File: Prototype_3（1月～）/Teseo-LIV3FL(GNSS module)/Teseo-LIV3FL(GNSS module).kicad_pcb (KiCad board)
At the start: 2 copper layers, 17 x 27.5 mm, 9 parts, among them IC1 TESEO-LIV3FL, J1 Conn_Coaxial, J2 Conn_01x05_Pin

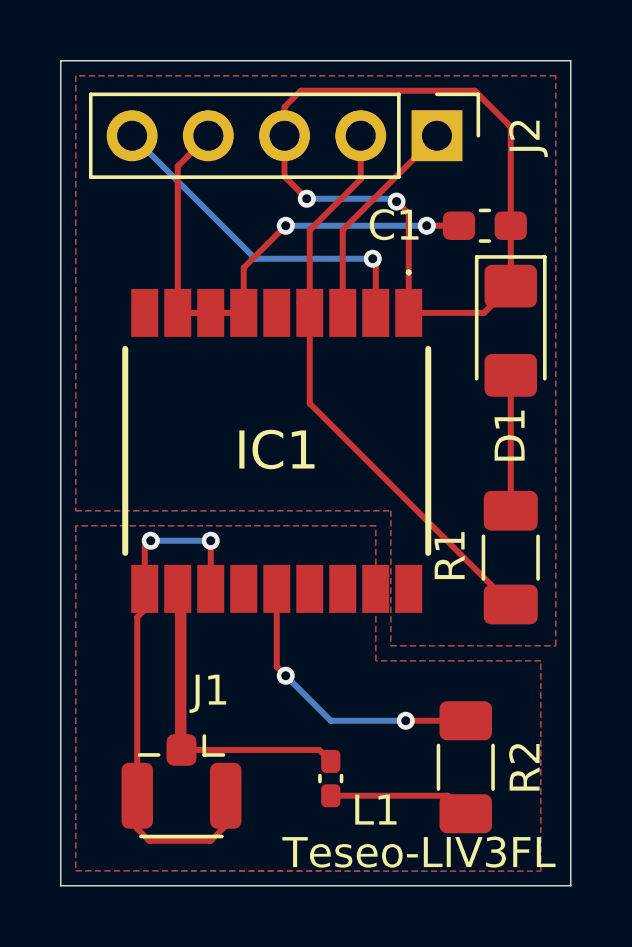
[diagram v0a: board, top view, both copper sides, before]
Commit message: Teseo
シルク印刷修正
- ピン名
シルク印刷追加
- LED Anode端子
- IC1 pin1丸印
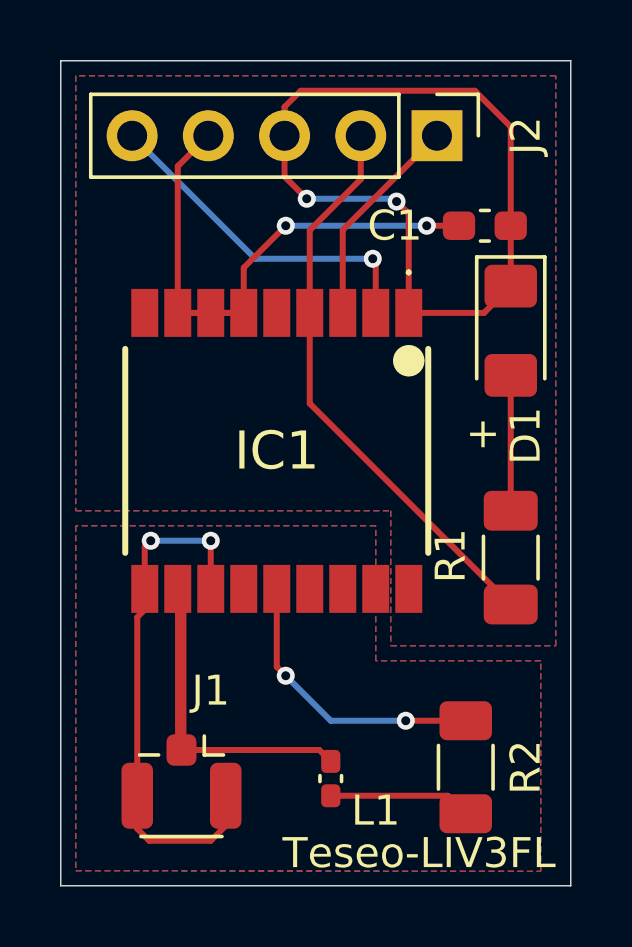
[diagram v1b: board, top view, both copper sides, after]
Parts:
- moved G*** 3.72 mm to (79.2, 71.4)
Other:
- board text added: "+"
- board text added: "PPS"
- board text removed: "1PPS"
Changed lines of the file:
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@@
 			(drillshape 0)
 			(scaleselection 1)
-			(outputdirectory "Teseo_jlcpcb/")
+			(outputdirectory "Teseo_gerber/")
 		)
 	)
@@
 		(tags "LED handsolder")
 		(property "Reference" "D1"
-			(at 3.5 0 90)
+			(at 3.5 -0.5 90)
 			(layer "F.SilkS")
 			(effects
@@
 	(footprint "library:REWRITE_logo"
 		(layer "B.Cu")
-		(at 75.761207 72.753171 -90)
+		(at 79.234181 71.432168 -90)
 		(property "Reference" "G***"
 			(at 0 0 90)
@@
 		(embedded_fonts no)
 	)
+	(gr_circle
+		(center 81.6 60)
+		(end 82.1 60)
+		(stroke
+			(width 0.05)
+			(type solid)
+		)
+		(fill yes)
+		(layer "F.SilkS")
+	)
 	(gr_rect
 		(start 70 50)
@@
 		(layer "Edge.Cuts")
 	)
+	(gr_text "+"
+		(at 83.5 63.005 0)
+		(layer "F.SilkS")
+		(effects
+			(font
+				(size 1 1)
+				(thickness 0.15)
+			)
+			(justify left bottom)
+		)
+	)
 	(gr_text "Teseo-LIV3FL"
 		(at 86.5 77 0)
@@
 		)
 	)
-	(gr_text "3V3"
+	(gr_text "GNSS-TX<->MCU-RX"
 		(at 73 55.5 90)
 		(layer "B.SilkS")
@@
 		)
 	)
-	(gr_text "GND"
+	(gr_text "3V3"
 		(at 75.5 55.5 90)
 		(layer "B.SilkS")
@@
 		)
 	)
-	(gr_text "1PPS"
+	(gr_text "GND"
 		(at 78 55.5 90)
 		(layer "B.SilkS")
@@
 		)
 	)
-	(gr_text "GNSS-RX<->MCU-TX"
+	(gr_text "PPS"
 		(at 80.5 55.5 90)
 		(layer "B.SilkS")
@@
 		)
 	)
-	(gr_text "GNSS-TX<->MCU-RX"
+	(gr_text "GNSS-RX<->MCU-TX"
 		(at 83.5 55.5 90)
 		(layer "B.SilkS")
